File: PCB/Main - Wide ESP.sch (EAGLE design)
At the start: 4 parts, among them U1 ESP32DEVKITC

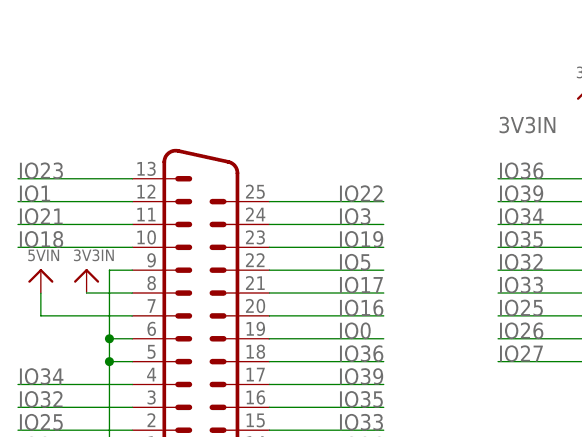
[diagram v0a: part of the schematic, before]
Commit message: Added exposed GND plane at DB25 anchors
All PCBs have been update to have exposed GND plane pads for the DB25 anchor points.

This resolves Issue 54
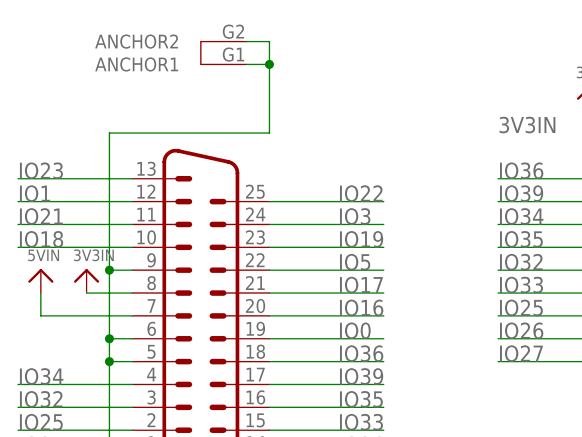
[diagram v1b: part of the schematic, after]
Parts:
- X1: device SparkFun-Retired:DB25_MALEH -> SparkFun-Retired:DB25_MALEHP
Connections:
- net GND: now also X1.ANCHOR1, X1.ANCHOR2
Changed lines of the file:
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@@
 </classes>
 <parts>
-<part name="X1" library="SparkFun-Retired" deviceset="DB25_MALE" device="H"/>
+<part name="X1" library="SparkFun-Retired" deviceset="DB25_MALE" device="HP"/>
 <part name="U$25" library="Airquality_Sensor" library_urn="urn:adsk.eagle:library:16015176" deviceset="GND" device=""/>
 <part name="U$27" library="microbuilder" deviceset="VIN" device="" value="5VIN"/>
@@
 <wire x1="233.68" y1="-12.7" x2="231.14" y2="-12.7" width="0.1524" layer="91"/>
 <junction x="231.14" y="-12.7"/>
+<wire x1="231.14" y1="-2.54" x2="231.14" y2="12.7" width="0.1524" layer="91"/>
+<junction x="231.14" y="-2.54"/>
+<wire x1="231.14" y1="12.7" x2="248.92" y2="12.7" width="0.1524" layer="91"/>
+<pinref part="X1" gate="-1" pin="ANCHOR2"/>
+<wire x1="248.92" y1="12.7" x2="248.92" y2="20.32" width="0.1524" layer="91"/>
+<wire x1="248.92" y1="20.32" x2="248.92" y2="22.86" width="0.1524" layer="91"/>
+<wire x1="248.92" y1="22.86" x2="246.38" y2="22.86" width="0.1524" layer="91"/>
+<pinref part="X1" gate="-1" pin="ANCHOR1"/>
+<wire x1="246.38" y1="20.32" x2="248.92" y2="20.32" width="0.1524" layer="91"/>
+<junction x="248.92" y="20.32"/>
 </segment>
 <segment>
